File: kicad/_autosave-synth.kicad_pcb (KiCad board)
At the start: 2 copper layers, 154.9 x 102.9 mm, 299 parts, among them CON101 SD_Card, CON201 K375A (DJK-02A), J301 KATE_3.5MM_6, J302 KATE_3.5MM_6, J401 KATE_3.5MM_6, J402 KATE_3.5MM_6, J403 KATE_3.5MM_6, P101 CONN_01X05, P102 CONN_01X03, P103 CONN_01X03, P104 47346-0001, P105 CONN_01X01, P106 DIN_5, P301 CONN_02X04, P302 CONN_01X03, Q101 MMBTA42, Q201 FDS6675, Q202 IRF7313PBF, Q301 Si2301DS, Q302 BC817, Q401 Si2301DS, Q402 Si2301DS, Q403 Si2301DS, SW101 SW_PUSH, SW102 SW_PUSH, T201 TRANS_CUSTOM, U101 STM32F405R, U102 USBLC6-2, U103 AD1955, U104 HCPL0453, U201 LM78L12ACZ, U202 79L12, U203 MC33269-SO8, U204 TPS76333DBV, U205 LP2985LV, U206 LP2985LV, U301 OP275S, U302 OP275S, U303 LM4864, U304 LM4864, U305 OP275S, U401 AD824, Y101 25MHz

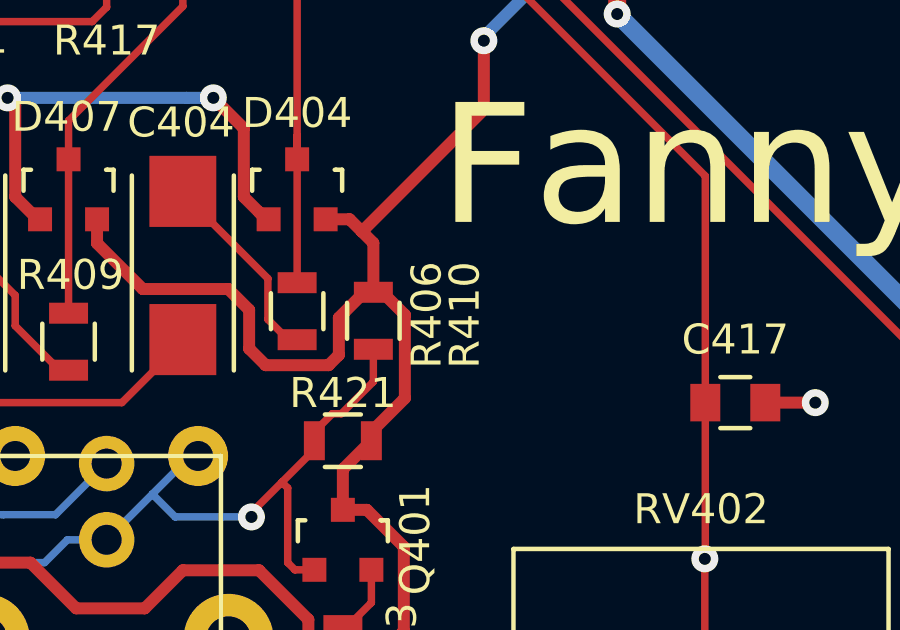
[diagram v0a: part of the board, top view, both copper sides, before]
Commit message: fixed p-mosfets
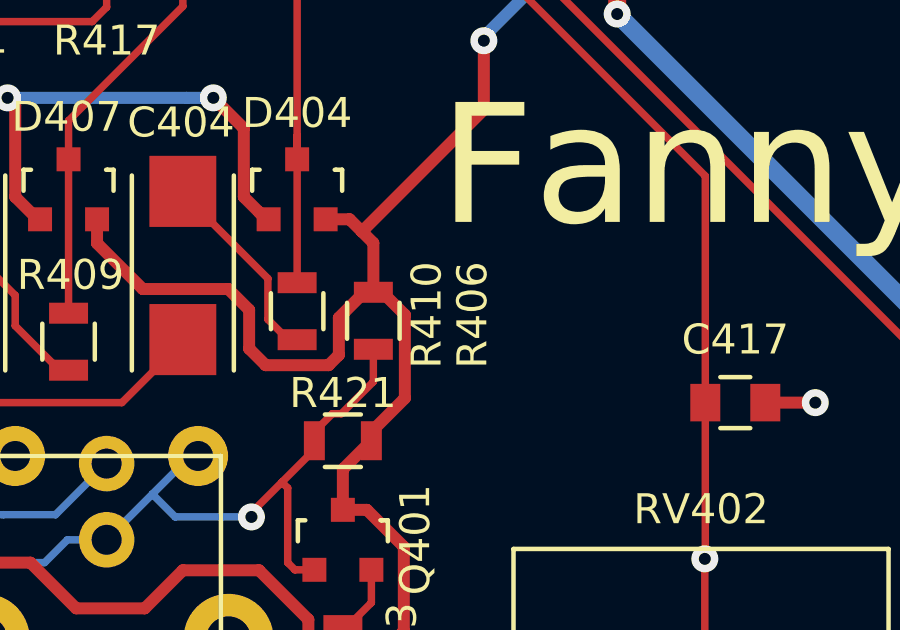
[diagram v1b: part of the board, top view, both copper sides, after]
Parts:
- C416, C417: value 1.0 -> 0.1
- R112, R114: value 47K -> 10K
- R113: value 47K -> N/C
- R339: value 10K -> 330
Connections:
- Q301 pad 2: Net-(Q301-Pad2) -> /audioout/+5VHEAD
- Q301 pad 3: /audioout/+5VHEAD -> Net-(Q301-Pad3)
- Q401 pad 2: Net-(Q401-Pad2) -> +3V3A_CPU
- Q401 pad 3: +3V3A_CPU -> Net-(Q401-Pad3)
- Q402 pad 2: Net-(Q402-Pad2) -> +3V3A_CPU
- Q402 pad 3: +3V3A_CPU -> Net-(Q402-Pad3)
- Q403 pad 2: Net-(Q403-Pad2) -> +3V3A_CPU
- Q403 pad 3: +3V3A_CPU -> Net-(Q403-Pad3)
- R304 pad 1: Net-(Q301-Pad2) -> Net-(Q301-Pad3)
- R401 pad 2: Net-(Q402-Pad2) -> Net-(Q402-Pad3)
- R402 pad 2: Net-(Q403-Pad2) -> Net-(Q403-Pad3)
- R403 pad 2: Net-(Q401-Pad2) -> Net-(Q401-Pad3)
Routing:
- net +3V3A_CPU: track 280.2 -> 244.2 mm
- net Net-(Q402-Pad3): track 0.00 -> 21.6 mm
- net Net-(Q301-Pad3): track 0.00 -> 20.2 mm
- net /audioout/+5VHEAD: track 93.3 -> 75.2 mm
- net Net-(Q403-Pad3): track 0.00 -> 17.2 mm
- net Net-(Q401-Pad3): track 0.00 -> 5.16 mm
- net Net-(Q402-Pad2): track 3.04 -> 0.00 mm
- net Net-(Q403-Pad2): track 2.51 -> 0.00 mm
- net Net-(Q401-Pad2): track 2.36 -> 0.00 mm
- net Net-(Q301-Pad2): track 2.14 -> 0.00 mm
